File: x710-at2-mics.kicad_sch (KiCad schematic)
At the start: 59 parts, among them U4 EZX710AT2_S_LMR5, U5 74LVC1G07_SOT-753

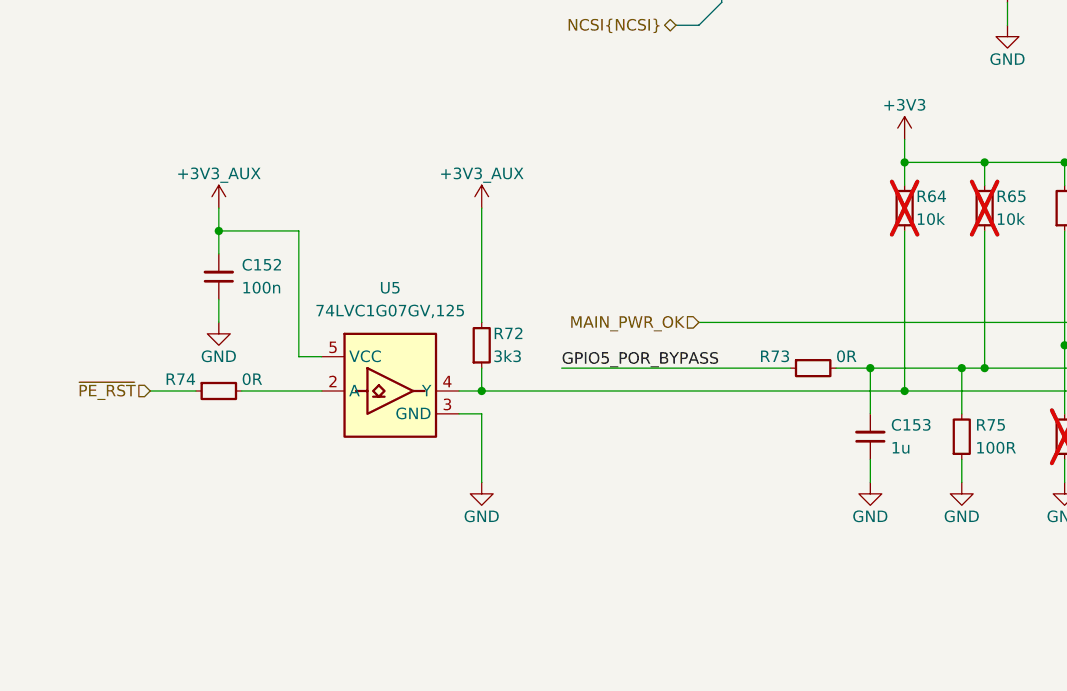
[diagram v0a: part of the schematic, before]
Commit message: [#80813] Add power input connectors, heatsink, mounting, draft component placement
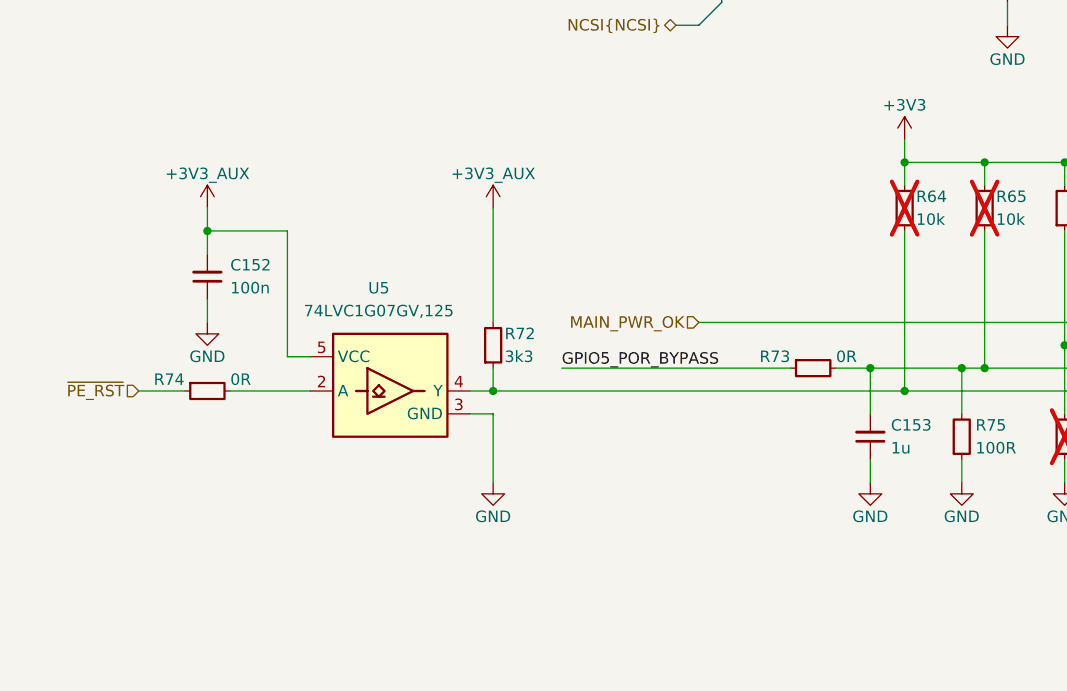
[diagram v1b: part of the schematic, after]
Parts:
- R50, R64, R65, R67, R76, R77, R78: now left out of the parts list
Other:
- moved on the sheet: C152, R72, R74

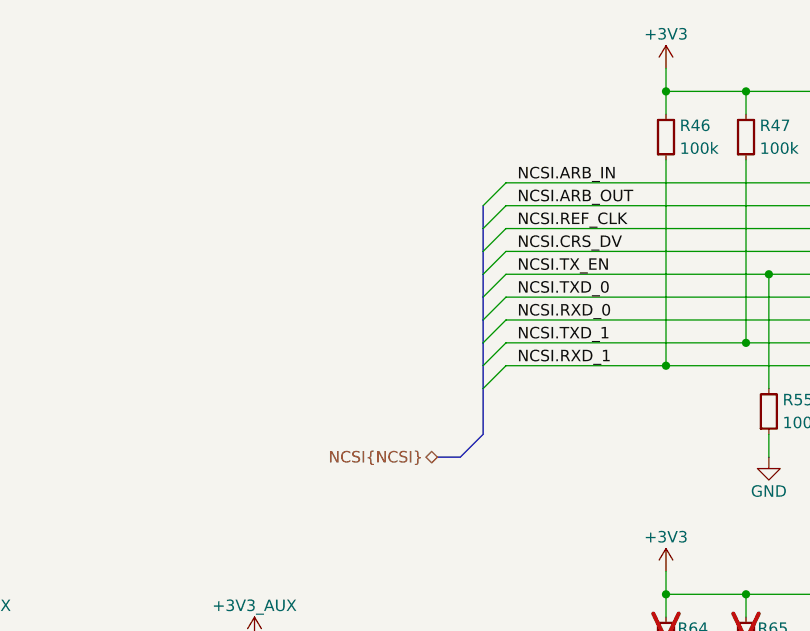
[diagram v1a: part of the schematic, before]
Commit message: [#80813] Change PCB mounts, replace NCSI connector with testpoints
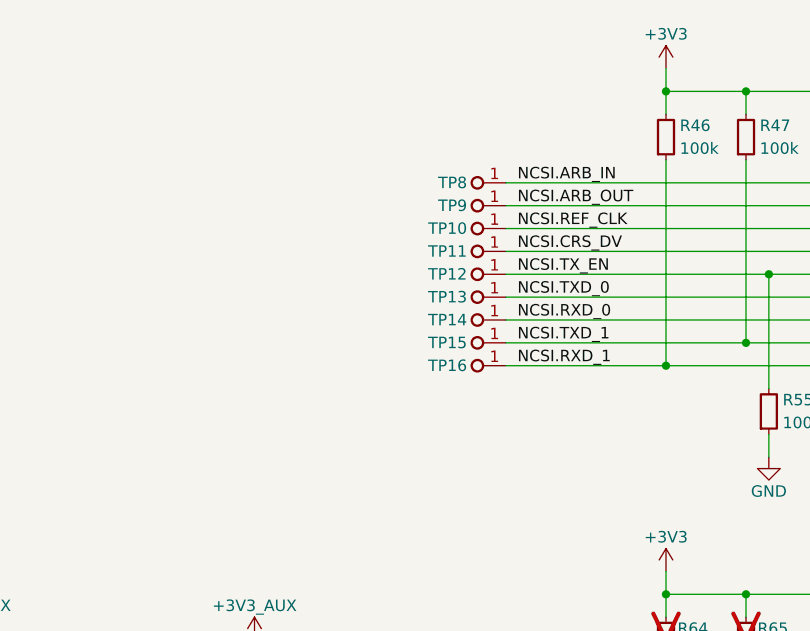
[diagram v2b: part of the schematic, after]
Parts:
- added TP10, TP11, TP12, TP13, TP14, TP15, TP16, TP8, TP9: TP_0.75mm_SMD, antmicro-footprints:TP_SMD_0.75mm, symbol antmicroTestPoints:TP_0.75mm_SMD
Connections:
- net NCSI.ARB_IN: now also TP8.1
- net NCSI.ARB_OUT: now also TP9.1
- net NCSI.CRS_DV: now also TP11.1
- net NCSI.REF_CLK: now also TP10.1
- net NCSI.RXD_0: now also TP14.1
- net NCSI.RXD_1: now also TP16.1
- net NCSI.TXD_0: now also TP13.1
- net NCSI.TXD_1: now also TP15.1
- net NCSI.TX_EN: now also TP12.1

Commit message: [#81595] Update symbols from library
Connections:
- no-connect marks 15 -> 34
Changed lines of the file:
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@@
 	)
 	(no_connect
+		(at 238.76 238.76)
+	)
+	(no_connect
 		(at 238.76 185.42)
 	)
@@
 	)
 	(no_connect
+		(at 238.76 233.68)
+	)
+	(no_connect
 		(at 182.88 175.26)
 	)
@@
 	)
 	(no_connect
+		(at 233.68 83.82)
+	)
+	(no_connect
 		(at 238.76 175.26)
 	)
 	(no_connect
+		(at 182.88 182.88)
+	)
+	(no_connect
 		(at 238.76 195.58)
 	)
@@
 	)
 	(no_connect
+		(at 238.76 236.22)
+	)
+	(no_connect
+		(at 182.88 180.34)
+	)
+	(no_connect
 		(at 182.88 172.72)
 	)
 	(no_connect
+		(at 182.88 200.66)
+	)
+	(no_connect
 		(at 238.76 200.66)
 	)
 	(no_connect
+		(at 182.88 205.74)
+	)
+	(no_connect
+		(at 238.76 231.14)
+	)
+	(no_connect
 		(at 238.76 170.18)
 	)
 	(no_connect
+		(at 238.76 246.38)
+	)
+	(no_connect
+		(at 182.88 198.12)
+	)
+	(no_connect
 		(at 182.88 167.64)
 	)
 	(no_connect
+		(at 233.68 76.2)
+	)
+	(no_connect
 		(at 238.76 187.96)
 	)
 	(no_connect
+		(at 238.76 226.06)
+	)
+	(no_connect
+		(at 238.76 243.84)
+	)
+	(no_connect
+		(at 238.76 228.6)
+	)
+	(no_connect
 		(at 238.76 193.04)
 	)
 	(no_connect
+		(at 182.88 203.2)
+	)
+	(no_connect
 		(at 238.76 180.34)
 	)
+	(no_connect
+		(at 233.68 81.28)
+	)
+	(no_connect
+		(at 238.76 223.52)
+	)
+	(no_connect
+		(at 238.76 241.3)
+	)
 	(bus_entry
 		(at 140.97 162.56)
@@
 	)
 	(symbol
-		(lib_name "EZX710AT2_S_LMR5_1")
 		(lib_id "antmicroInterfaceControllers:EZX710AT2_S_LMR5")
 		(at 182.88 160.02 0)

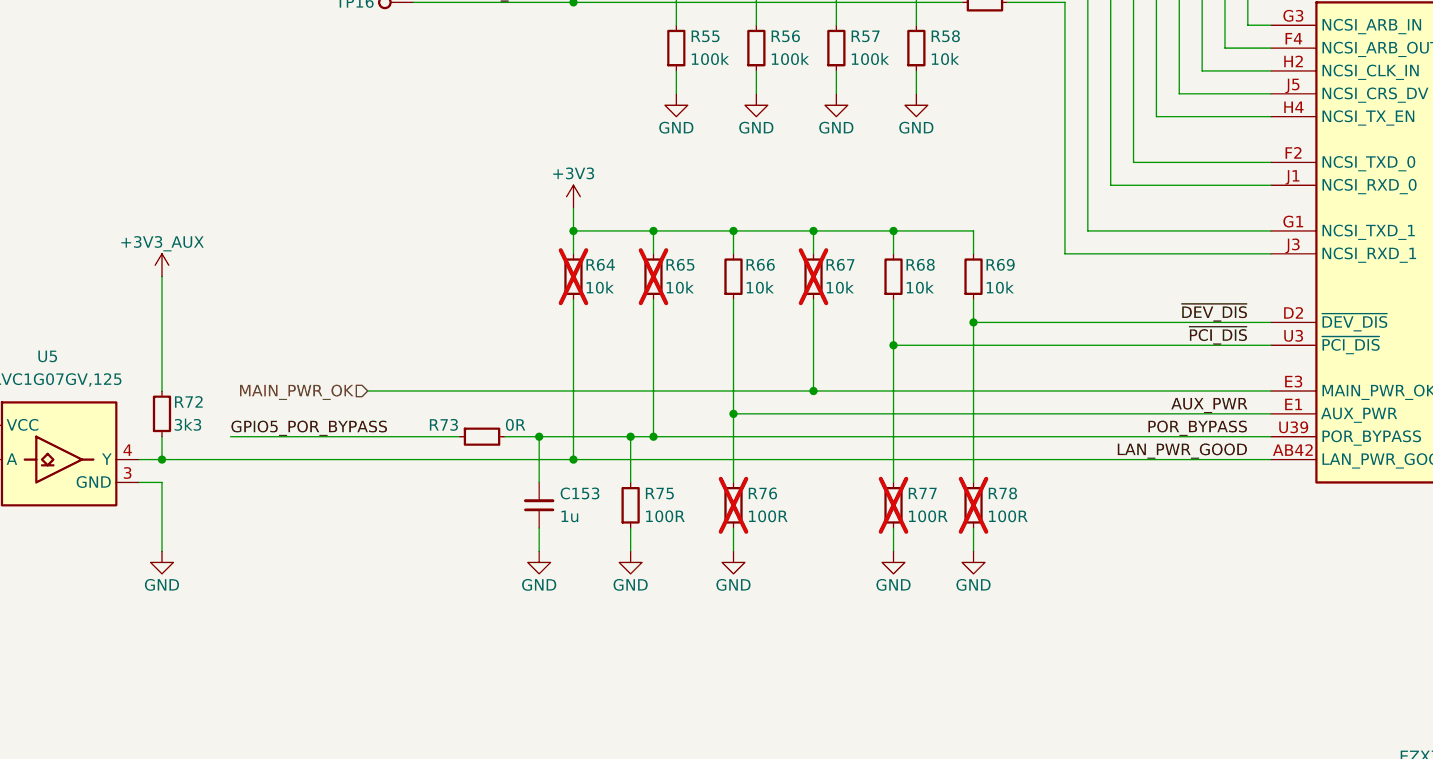
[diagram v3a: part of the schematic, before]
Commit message: [#81595] WIP: Connect remaining control signals
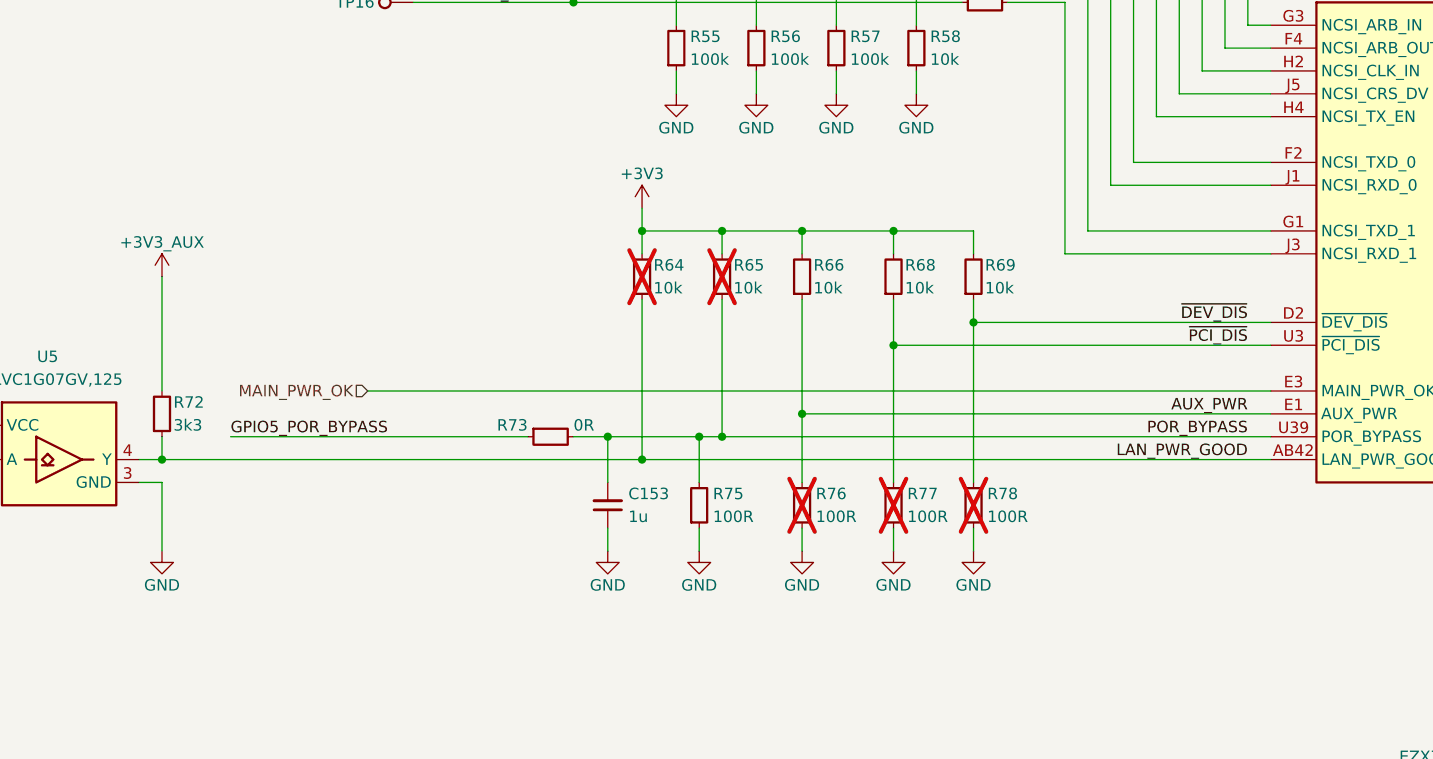
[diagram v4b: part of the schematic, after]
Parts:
- removed R67: R_10k_0402, antmicro-footprints:R_0402_1005Metric, symbol antmicroResistors0402:R_10k_0402
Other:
- moved on the sheet: C153, R64, R65, R66, R73, R75, R76

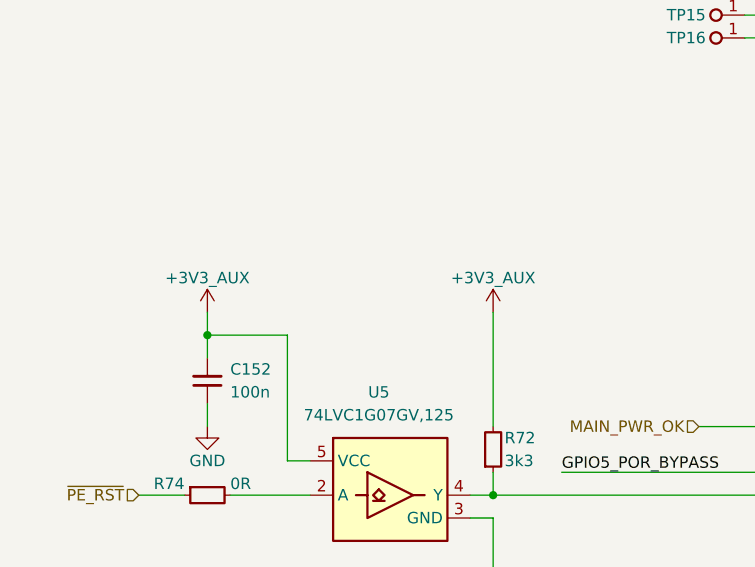
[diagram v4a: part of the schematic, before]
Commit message: [#85196] Clear ERC, minor schematic fixes
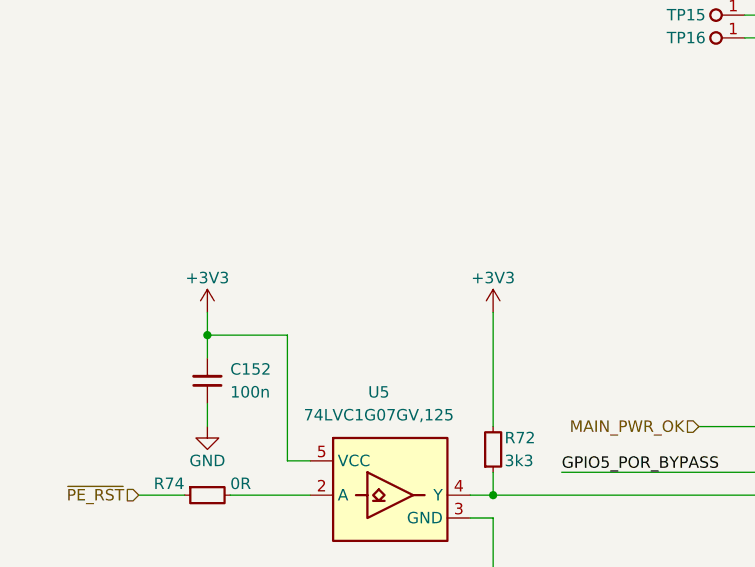
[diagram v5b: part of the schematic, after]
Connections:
- net +3V3_AUX is gone; now on net +3V3: C152.2, R72.2, U5.5 (VCC)
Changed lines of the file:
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@@
 	)
 	(symbol
-		(lib_id "antmicropower:VCC")
-		(at 64.77 101.6 0)
-		(unit 1)
-		(exclude_from_sim no)
-		(in_bom yes)
-		(on_board yes)
-		(dnp no)
-		(property "Reference" "#PWR0211"
-			(at 64.77 105.41 0)
-			(effects
-				(font
-					(size 1.27 1.27)
-				)
-				(hide yes)
-			)
-		)
-		(property "Value" "+3V3_AUX"
-			(at 64.77 97.79 0)
-			(effects
-				(font
-					(size 1.27 1.27)
-				)
-			)
-		)
-		(property "Footprint" ""
-			(at 64.77 101.6 0)
-			(effects
-				(font
-					(size 1.27 1.27)
-				)
-				(hide yes)
-			)
-		)
-		(property "Datasheet" ""
-			(at 64.77 101.6 0)
-			(effects
-				(font
-					(size 1.27 1.27)
-				)
-				(hide yes)
-			)
-		)
-		(property "Description" ""
-			(at 64.77 101.6 0)
-			(effects
-				(font
-					(size 1.27 1.27)
-				)
-				(hide yes)
-			)
-		)
-		(pin "1"
-		)
-		(instances
-			(project "10-gbe-expansion"
-				(path "/04bda987-e5eb-48b4-9e90-d8211dc11b39/d0402c84-6d4c-4559-b85a-0c9b588a21c5"
-					(reference "#PWR0211")
-					(unit 1)
-				)
-			)
-		)
-	)
-	(symbol
 		(lib_id "antmicropower:GND")
 		(at 276.86 246.38 0)
@@
 	)
 	(symbol
+		(lib_id "antmicropower:+3V3")
+		(at 33.02 101.6 0)
+		(unit 1)
+		(exclude_from_sim no)
+		(in_bom yes)
+		(on_board yes)
+		(dnp no)
+		(property "Reference" "#PWR0210"
+			(at 48.26 101.6 0)
+			(effects
+				(font
+					(size 1.27 1.27)
+					(thickness 0.15)
+				)
+				(justify left bottom)
+				(hide yes)
+			)
+		)
+		(property "Value" "+3V3"
+			(at 33.02 97.79 0)
+			(effects
+				(font
+					(size 1.27 1.27)
+					(thickness 0.15)
+				)
+			)
+		)
+		(property "Footprint" ""
+			(at 48.26 109.22 0)
+			(effects
+				(font
+					(size 1.27 1.27)
+					(thickness 0.15)
+				)
+				(justify left bottom)
+				(hide yes)
+			)
+		)
+		(property "Datasheet" ""
+			(at 48.26 111.76 0)
+			(effects
+				(font
+					(size 1.27 1.27)
+					(thickness 0.15)
+				)
+				(justify left bottom)
+				(hide yes)
+			)
+		)
+		(property "Description" ""
+			(at 33.02 101.6 0)
+			(effects
+				(font
+					(size 1.27 1.27)
+				)
+				(hide yes)
+			)
+		)
+		(property "Author" "Antmicro"
+			(at 48.26 104.14 0)
+			(effects
+				(font
+					(size 1.27 1.27)
+					(thickness 0.15)
+				)
+				(justify left bottom)
+				(hide yes)
+			)
+		)
+		(property "License" "Apache-2.0"
+			(at 48.26 106.68 0)
+			(effects
+				(font
+					(size 1.27 1.27)
+					(thickness 0.15)
+				)
+				(justify left bottom)
+				(hide yes)
+			)
+		)
+		(pin "1"
+		)
+		(instances
+			(project "10-gbe-expansion"
+				(path "/04bda987-e5eb-48b4-9e90-d8211dc11b39/d0402c84-6d4c-4559-b85a-0c9b588a21c5"
+					(reference "#PWR0210")
+					(unit 1)
+				)
+			)
+		)
+	)
+	(symbol
 		(lib_id "antmicroTestPoints:TP_0.75mm_SMD")
 		(at 170.18 226.06 180)
@@
 	)
 	(symbol
+		(lib_id "antmicropower:+3V3")
+		(at 64.77 101.6 0)
+		(unit 1)
+		(exclude_from_sim no)
+		(in_bom yes)
+		(on_board yes)
+		(dnp no)
+		(property "Reference" "#PWR0211"
+			(at 80.01 101.6 0)
+			(effects
+				(font
+					(size 1.27 1.27)
+					(thickness 0.15)
+				)
+				(justify left bottom)
+				(hide yes)
+			)
+		)
+		(property "Value" "+3V3"
+			(at 64.77 97.79 0)
+			(effects
+				(font
+					(size 1.27 1.27)
+					(thickness 0.15)
+				)
+			)
+		)
+		(property "Footprint" ""
+			(at 80.01 109.22 0)
+			(effects
+				(font
+					(size 1.27 1.27)
+					(thickness 0.15)
+				)
+				(justify left bottom)
+				(hide yes)
+			)
+		)
+		(property "Datasheet" ""
+			(at 80.01 111.76 0)
+			(effects
+				(font
+					(size 1.27 1.27)
+					(thickness 0.15)
+				)
+				(justify left bottom)
+				(hide yes)
+			)
+		)
+		(property "Description" ""
+			(at 64.77 101.6 0)
+			(effects
+				(font
+					(size 1.27 1.27)
+				)
+				(hide yes)
+			)
+		)
+		(property "Author" "Antmicro"
+			(at 80.01 104.14 0)
+			(effects
+				(font
+					(size 1.27 1.27)
+					(thickness 0.15)
+				)
+				(justify left bottom)
+				(hide yes)
+			)
+		)
+		(property "License" "Apache-2.0"
+			(at 80.01 106.68 0)
+			(effects
+				(font
+					(size 1.27 1.27)
+					(thickness 0.15)
+				)
+				(justify left bottom)
+				(hide yes)
+			)
+		)
+		(pin "1"
+		)
+		(instances
+			(project "10-gbe-expansion"
+				(path "/04bda987-e5eb-48b4-9e90-d8211dc11b39/d0402c84-6d4c-4559-b85a-0c9b588a21c5"
+					(reference "#PWR0211")
+					(unit 1)
+				)
+			)
+		)
+	)
+	(symbol
 		(lib_id "antmicroResistors0402:R_10k_0402")
 		(at 274.32 96.52 90)
@@
 					(unit 1)
 				)
-			)
-		)
-	)
-	(symbol
-		(lib_id "antmicropower:VCC")
-		(at 33.02 101.6 0)
-		(unit 1)
-		(exclude_from_sim no)
-		(in_bom yes)
-		(on_board yes)
-		(dnp no)
-		(property "Reference" "#PWR0210"
-			(at 33.02 105.41 0)
-			(effects
-				(font
-					(size 1.27 1.27)
-				)
-				(hide yes)
-			)
-		)
-		(property "Value" "+3V3_AUX"
-			(at 33.02 97.79 0)
-			(effects
-				(font
-					(size 1.27 1.27)
-				)
-			)
-		)
-		(property "Footprint" ""
-			(at 33.02 101.6 0)
-			(effects
-				(font
-					(size 1.27 1.27)
-				)
-				(hide yes)
-			)
-		)
-		(property "Datasheet" ""
-			(at 33.02 101.6 0)
-			(effects
-				(font
-					(size 1.27 1.27)
-				)
-				(hide yes)
-			)
-		)
-		(property "Description" ""
-			(at 33.02 101.6 0)
-			(effects
-				(font
-					(size 1.27 1.27)
-				)
-				(hide yes)
-			)
-		)
-		(pin "1"
-		)
-		(instances
-			(project "10-gbe-expansion"
-				(path "/04bda987-e5eb-48b4-9e90-d8211dc11b39/d0402c84-6d4c-4559-b85a-0c9b588a21c5"
-					(reference "#PWR0210")
-					(unit 1)
-				)

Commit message: [#85196] Re-annotate schematic
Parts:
- renumbered C152 to C198, C153 to C199, R69 to R100, R70 to R101, R71 to R102, R72 to R103, R73 to R104, R74 to R105, R75 to R106, R76 to R107, R77 to R108, R78 to R109, R79 to R110, R80 to R111, R81 to R112, R82 to R113, R83 to R114, R84 to R115, R85 to R116, R86 to R117, R87 to R118, R88 to R119, R89 to R120, R90 to R121, R91 to R122, R92 to R123, R93 to R124, R94 to R125, R95 to R126, R96 to R127, R46 to R78, R47 to R79, R48 to R80, R49 to R81, R50 to R82, R51 to R83, R52 to R84, R53 to R85, R54 to R86, R55 to R87, R56 to R88, R57 to R89, R58 to R90, R59 to R91, R60 to R92, R61 to R93, R62 to R94, R63 to R95, R64 to R96, R65 to R97, R66 to R98, R68 to R99, TP8 to TP1, TP1 to TP10, TP2 to TP11, TP3 to TP12, TP4 to TP13, TP9 to TP2, TP10 to TP3, TP11 to TP4, TP12 to TP5, TP13 to TP6, TP14 to TP7, TP15 to TP8, TP16 to TP9, U5 to U10, U4 to U9
